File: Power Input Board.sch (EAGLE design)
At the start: 9 parts, among them Q1 SPB80P06P

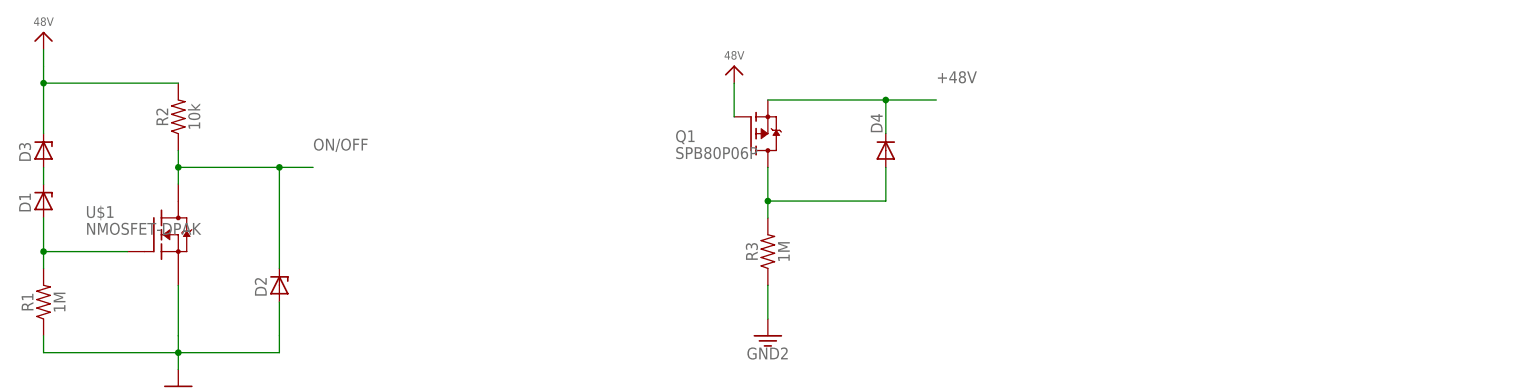
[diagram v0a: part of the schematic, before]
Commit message: added board outline
added the board outline
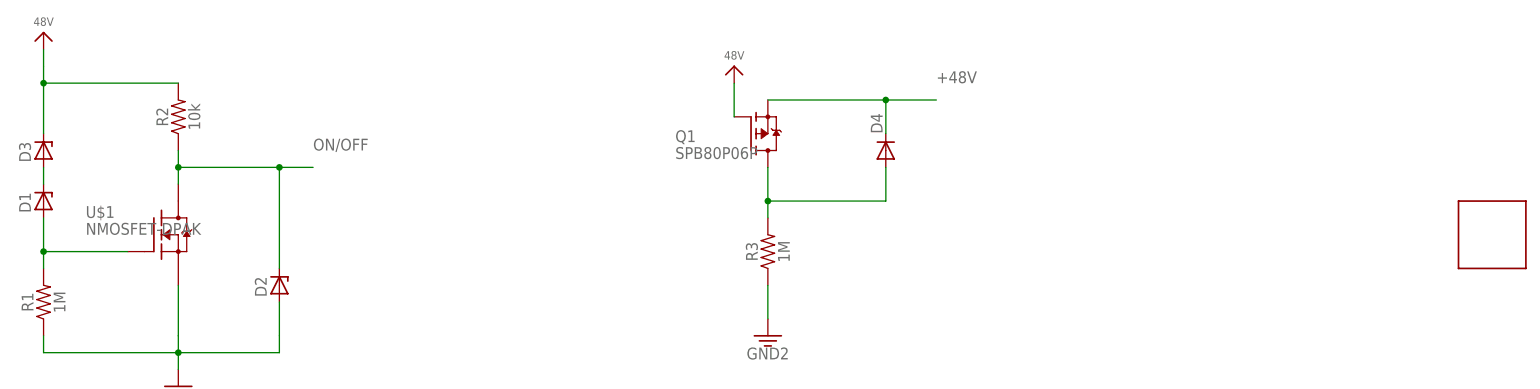
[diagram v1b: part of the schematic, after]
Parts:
- added U$2: BOARDPDB, board_outlines:BOARDPDB
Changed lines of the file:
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@@
 <?xml version="1.0" encoding="utf-8"?>
 <!DOCTYPE eagle SYSTEM "eagle.dtd">
-<eagle version="9.1.3">
+<eagle version="9.2.0">
 <drawing>
 <settings>
@@
 <part name="+48V" library="audio amplifier example" library_urn="urn:adsk.eagle:library:970892" deviceset="VCC" device="" value="48V"/>
 <part name="Q1" library="transistor-fet" library_urn="urn:adsk.eagle:library:396" deviceset="SPB80P06P" device="" package3d_urn="urn:adsk.eagle:package:28539/2"/>
+<part name="U$2" library="board_outlines" deviceset="BOARD" device="PDB"/>
 </parts>
 <sheets>
@@
 </plain>
 <instances>
-<instance part="U$1" gate="G$1" x="55.88" y="198.12"/>
-<instance part="D1" gate="G$1" x="38.1" y="203.2" rot="R90"/>
-<instance part="D2" gate="G$1" x="73.66" y="190.5" rot="R90"/>
-<instance part="D3" gate="G$1" x="38.1" y="210.82" rot="R90"/>
-<instance part="R1" gate="G$1" x="38.1" y="187.96" rot="R90"/>
-<instance part="R2" gate="G$1" x="58.42" y="215.9" rot="R90"/>
-<instance part="FRAME1" gate="G$1" x="0" y="0"/>
-<instance part="P+1" gate="VCC" x="38.1" y="228.6"/>
-<instance part="GND1" gate="G$1" x="58.42" y="175.26"/>
-<instance part="D4" gate="G$1" x="165.1" y="210.82" rot="R90"/>
-<instance part="R3" gate="G$1" x="147.32" y="195.58" rot="R90"/>
-<instance part="GND2" gate="G$1" x="147.32" y="182.88"/>
-<instance part="+48V" gate="VCC" x="142.24" y="223.52"/>
-<instance part="Q1" gate="G$1" x="144.78" y="213.36"/>
+<instance part="U$1" gate="G$1" x="55.88" y="198.12">
+<attribute name="VALUE" x="44.45" y="198.12" size="1.778" layer="96"/>
+<attribute name="NAME" x="44.45" y="200.66" size="1.778" layer="95"/>
+</instance>
+<instance part="D1" gate="G$1" x="38.1" y="203.2" rot="R90">
+<attribute name="NAME" x="36.195" y="201.422" size="1.778" layer="95" rot="R90"/>
+<attribute name="VALUE" x="41.529" y="201.422" size="1.778" layer="96" rot="R90"/>
+</instance>
+<instance part="D2" gate="G$1" x="73.66" y="190.5" rot="R90">
+<attribute name="NAME" x="71.755" y="188.722" size="1.778" layer="95" rot="R90"/>
+<attribute name="VALUE" x="77.089" y="188.722" size="1.778" layer="96" rot="R90"/>
+</instance>
+<instance part="D3" gate="G$1" x="38.1" y="210.82" rot="R90">
+<attribute name="NAME" x="36.195" y="209.042" size="1.778" layer="95" rot="R90"/>
+<attribute name="VALUE" x="41.529" y="209.042" size="1.778" layer="96" rot="R90"/>
+</instance>
+<instance part="R1" gate="G$1" x="38.1" y="187.96" rot="R90">
+<attribute name="NAME" x="36.576" y="187.96" size="1.778" layer="95" font="vector" rot="R90" align="bottom-center"/>
+<attribute name="VALUE" x="39.624" y="187.96" size="1.778" layer="96" font="vector" rot="R90" align="top-center"/>
+</instance>
+<instance part="R2" gate="G$1" x="58.42" y="215.9" rot="R90">
+<attribute name="NAME" x="56.896" y="215.9" size="1.778" layer="95" font="vector" rot="R90" align="bottom-center"/>
+<attribute name="VALUE" x="59.944" y="215.9" size="1.778" layer="96" font="vector" rot="R90" align="top-center"/>
+</instance>
+<instance part="FRAME1" gate="G$1" x="0" y="0">
+<attribute name="DRAWING_NAME" x="344.17" y="15.24" size="2.54" layer="94"/>
+<attribute name="LAST_DATE_TIME" x="344.17" y="10.16" size="2.286" layer="94"/>
+<attribute name="SHEET" x="357.505" y="5.08" size="2.54" layer="94"/>
+</instance>
+<instance part="P+1" gate="VCC" x="38.1" y="228.6">
+<attribute name="VALUE" x="36.576" y="229.616" size="1.27" layer="96"/>
+</instance>
+<instance part="GND1" gate="G$1" x="58.42" y="175.26">
+<attribute name="VALUE" x="58.42" y="173.482" size="1.778" layer="96" align="top-center"/>
+</instance>
+<instance part="D4" gate="G$1" x="165.1" y="210.82" rot="R90">
+<attribute name="NAME" x="164.6174" y="213.36" size="1.778" layer="95" rot="R90"/>
+<attribute name="VALUE" x="167.4114" y="213.36" size="1.778" layer="96" rot="R90"/>
+</instance>
+<instance part="R3" gate="G$1" x="147.32" y="195.58" rot="R90">
+<attribute name="NAME" x="145.796" y="195.58" size="1.778" layer="95" font="vector" rot="R90" align="bottom-center"/>
+<attribute name="VALUE" x="148.844" y="195.58" size="1.778" layer="96" font="vector" rot="R90" align="top-center"/>
+</instance>
+<instance part="GND2" gate="G$1" x="147.32" y="182.88">
+<attribute name="VALUE" x="147.32" y="181.102" size="1.778" layer="96" align="top-center"/>
+</instance>
+<instance part="+48V" gate="VCC" x="142.24" y="223.52">
+<attribute name="VALUE" x="140.716" y="224.536" size="1.27" layer="96"/>
+</instance>
+<instance part="Q1" gate="G$1" x="144.78" y="213.36">
+<attribute name="VALUE" x="133.35" y="209.55" size="1.778" layer="96"/>
+<attribute name="NAME" x="133.35" y="212.09" size="1.778" layer="95"/>
+</instance>
+<instance part="U$2" gate="G$1" x="256.54" y="198.12"/>
 </instances>
 <busses>

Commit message: put in outline
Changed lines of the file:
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@@
 <attribute name="NAME" x="133.35" y="212.09" size="1.778" layer="95"/>
 </instance>
-<instance part="U$2" gate="G$1" x="256.54" y="198.12"/>
+<instance part="U$2" gate="G$1" x="215.9" y="241.3"/>
 </instances>
 <busses>

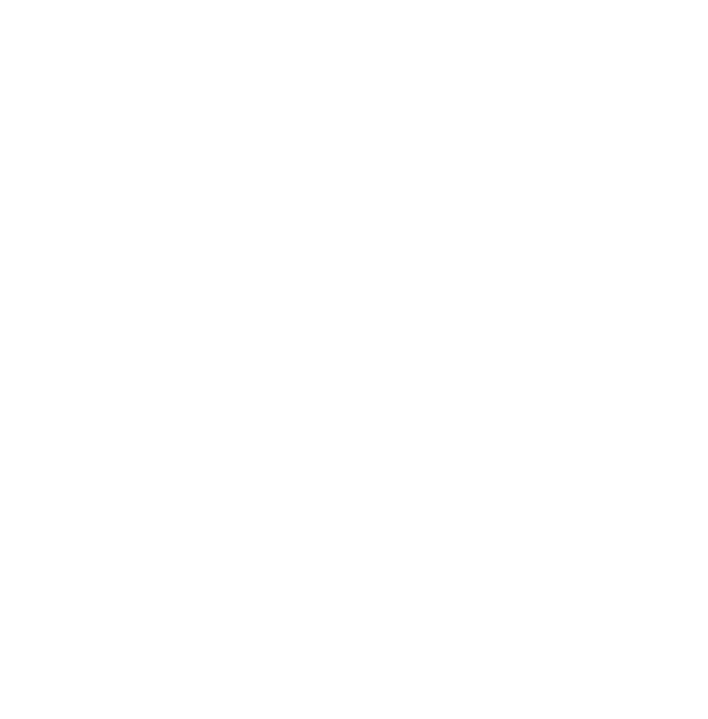
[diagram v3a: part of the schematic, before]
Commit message: inserted diodes
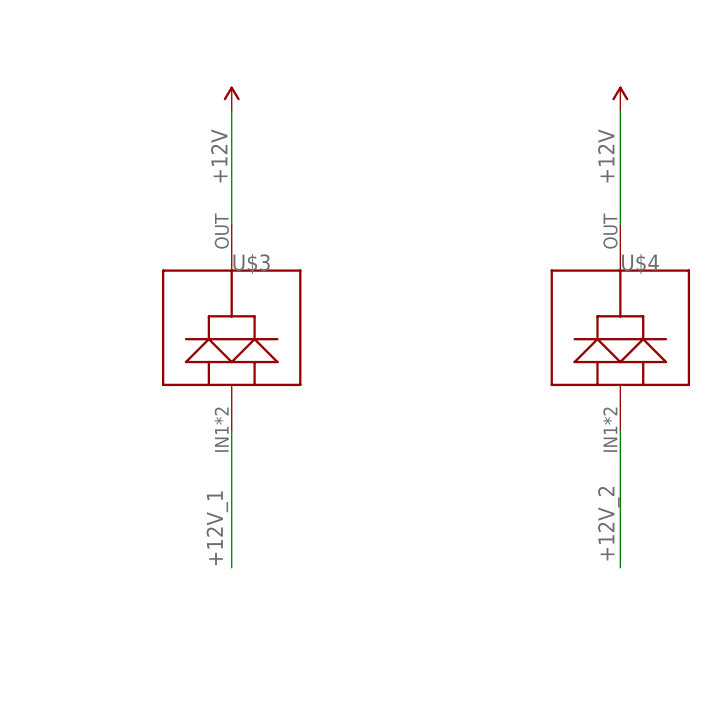
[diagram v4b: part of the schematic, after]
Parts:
- added U$3, U$4: DIODE, DIODE:DIODE
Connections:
- new net +12V: U$3.OUT, U$4.OUT
- new net +12V_1: U$3.IN2
- new net +12V_2: U$4.IN2
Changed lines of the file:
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@@
 <setting verticaltext="up"/>
 </settings>
-<grid distance="0.1" unitdist="inch" unit="inch" style="lines" multiple="1" display="no" altdistance="0.01" altunitdist="inch" altunit="inch"/>
+<grid distance="1" unitdist="mm" unit="mm" style="lines" multiple="1" display="no" altdistance="0.01" altunitdist="inch" altunit="inch"/>
 <layers>
 <layer number="1" name="Top" color="4" fill="1" visible="no" active="no"/>
@@
 <part name="Q1" library="transistor-fet" library_urn="urn:adsk.eagle:library:396" deviceset="SPB80P06P" device="" package3d_urn="urn:adsk.eagle:package:28539/2"/>
 <part name="U$2" library="board_outlines" deviceset="BOARD" device="PDB"/>
+<part name="U$3" library="DIODE" deviceset="DIODE" device=""/>
+<part name="U$4" library="DIODE" deviceset="DIODE" device=""/>
+<part name="SUPPLY1" library="SparkFun-PowerSymbols" library_urn="urn:adsk.eagle:library:530" deviceset="VCC" device="" value=""/>
+<part name="SUPPLY2" library="SparkFun-PowerSymbols" library_urn="urn:adsk.eagle:library:530" deviceset="VCC" device="" value=""/>
 </parts>
 <sheets>
@@
 </instance>
 <instance part="U$2" gate="G$1" x="215.9" y="241.3"/>
+<instance part="U$3" gate="G$1" x="284.48" y="213.36"/>
+<instance part="U$4" gate="G$1" x="327.66" y="213.36"/>
+<instance part="SUPPLY1" gate="G$1" x="284.48" y="236.22"/>
+<instance part="SUPPLY2" gate="G$1" x="327.66" y="236.22"/>
 </instances>
 <busses>
@@
 </segment>
 </net>
+<net name="+12V_1" class="0">
+<segment>
+<pinref part="U$3" gate="G$1" pin="IN2"/>
+<wire x1="284.48" y1="200.66" x2="284.48" y2="185.42" width="0.1524" layer="91"/>
+<label x="283.5" y="185.48" size="1.778" layer="95" rot="R90"/>
+</segment>
+</net>
+<net name="+12V_2" class="0">
+<segment>
+<pinref part="U$4" gate="G$1" pin="IN2"/>
+<wire x1="327.66" y1="200.66" x2="327.66" y2="185.42" width="0.1524" layer="91"/>
+<label x="327" y="186" size="1.778" layer="95" rot="R90"/>
+</segment>
+</net>
+<net name="+12V" class="0">
+<segment>
+<pinref part="U$3" gate="G$1" pin="OUT"/>
+<wire x1="284.48" y1="223.52" x2="284.48" y2="236.22" width="0.1524" layer="91"/>
+<pinref part="SUPPLY1" gate="G$1" pin="VCC"/>
+<label x="284" y="228" size="1.778" layer="95" rot="R90"/>
+</segment>
+<segment>
+<pinref part="U$4" gate="G$1" pin="OUT"/>
+<wire x1="327.66" y1="223.52" x2="327.66" y2="236.22" width="0.1524" layer="91"/>
+<pinref part="SUPPLY2" gate="G$1" pin="VCC"/>
+<label x="327" y="228" size="1.778" layer="95" rot="R90"/>
+</segment>
+</net>

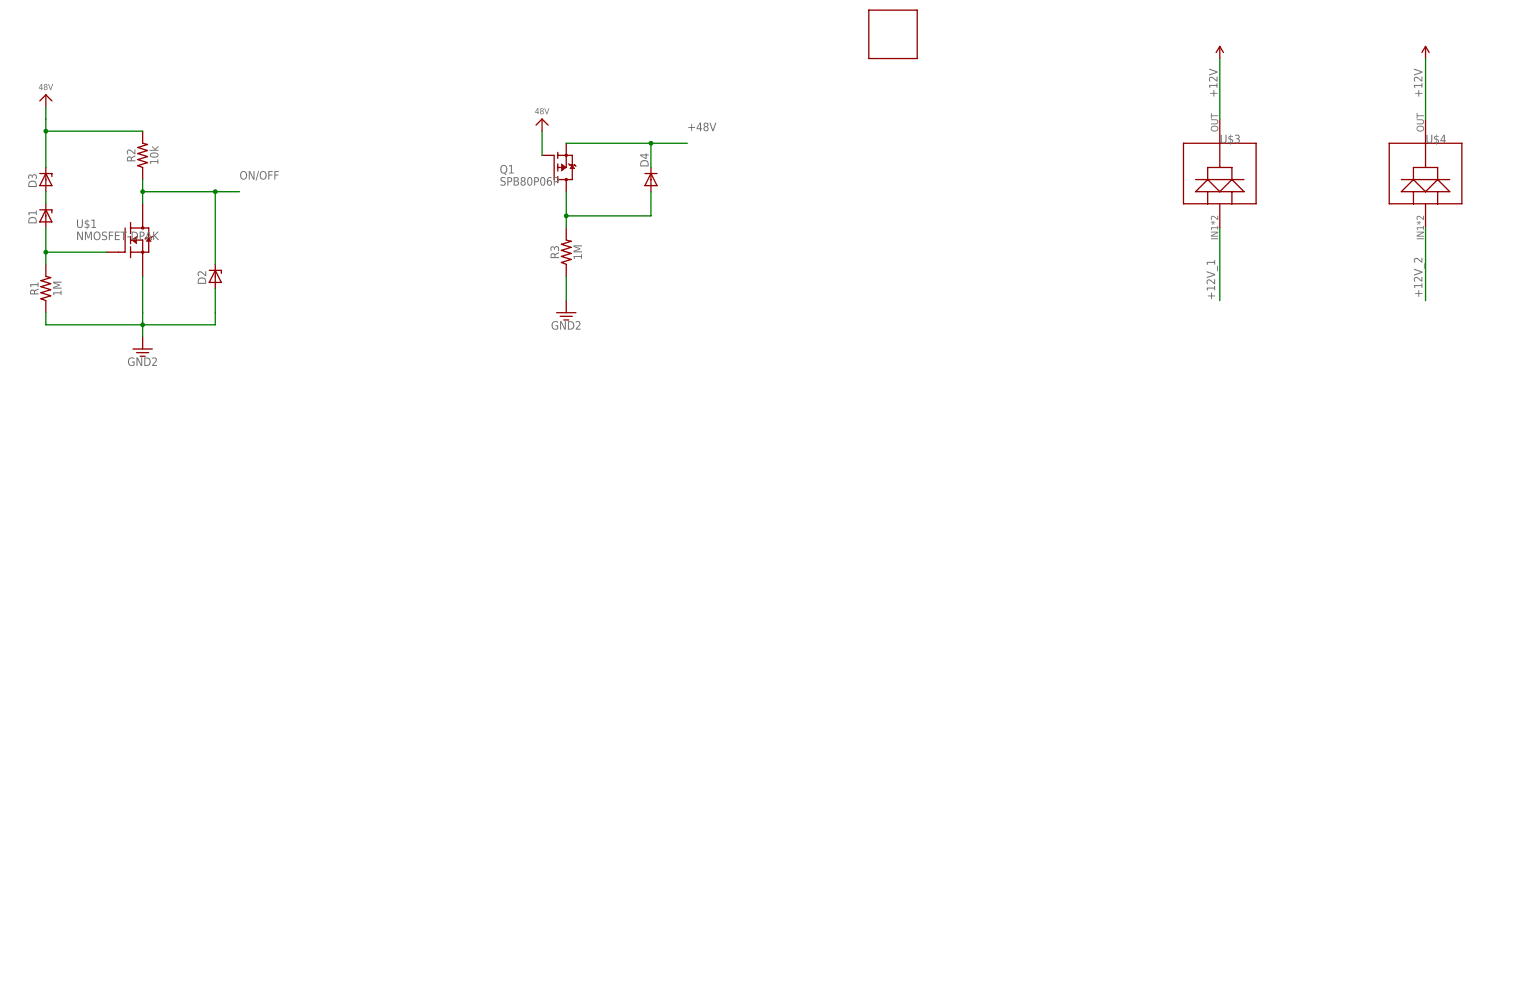
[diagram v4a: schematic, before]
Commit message: put the connectors on the board
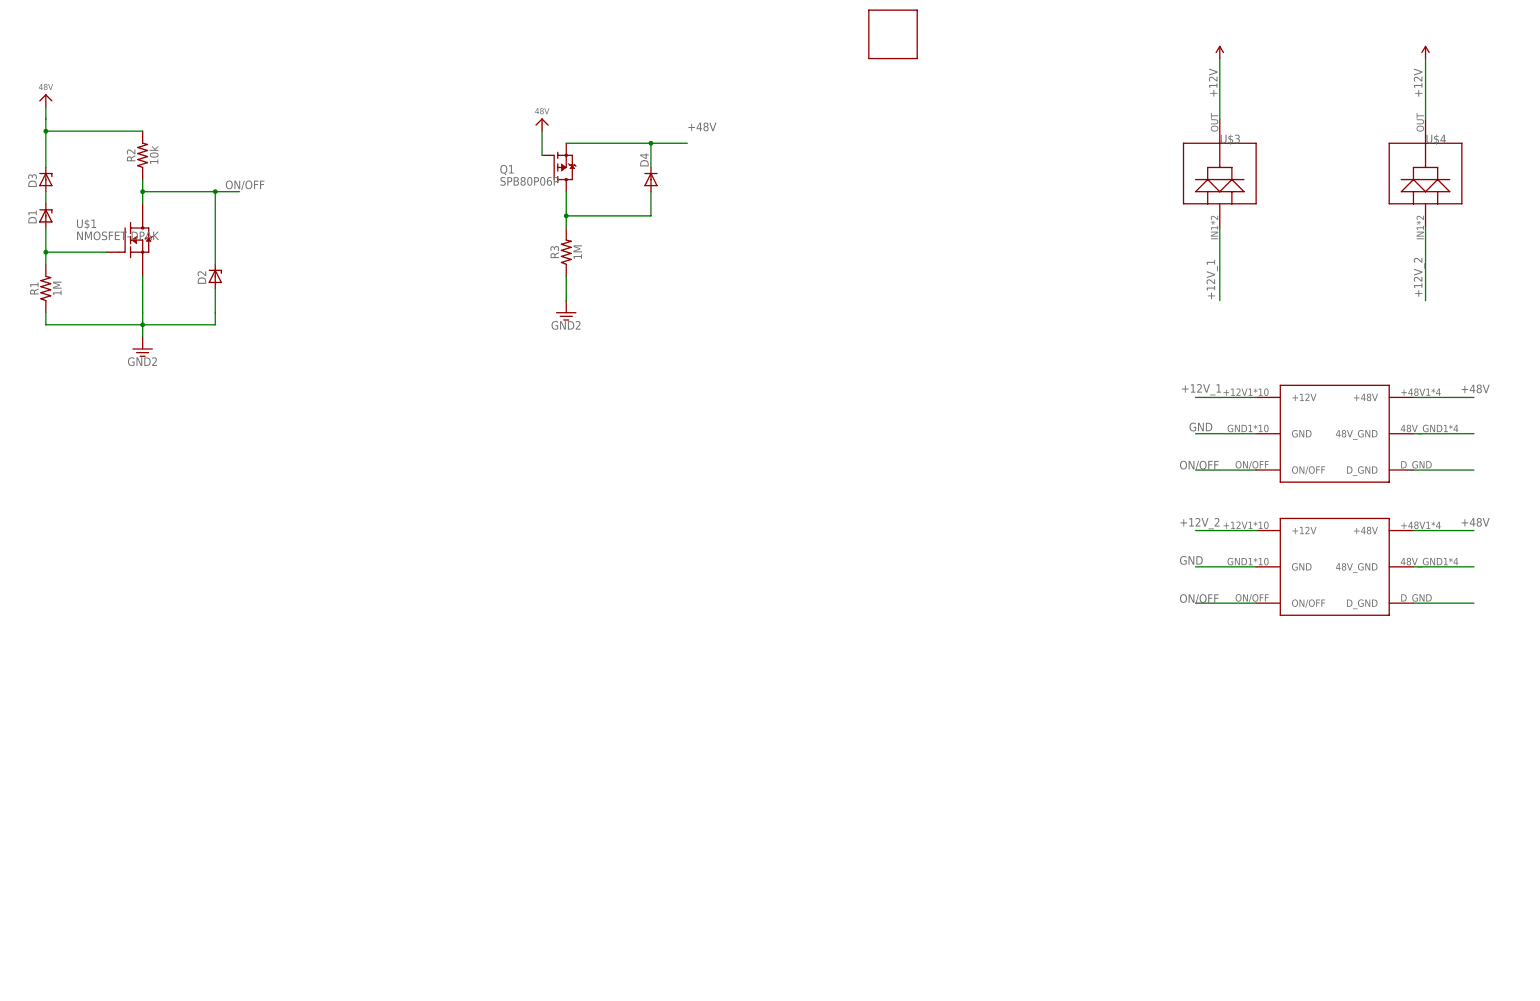
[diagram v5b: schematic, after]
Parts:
- added U$5, U$6: BRICK_TO_POWER_DIST_WHOLE, PDB_TO_BRICKS:BRICK_TO_POWER_DIST_WHOLE
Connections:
- new net GND: U$5.GND, U$6.GND
- new net N$10: U$5.D_GND
- new net N$12: U$6.48V_GND
- new net N$13: U$6.D_GND
- new net N$9: U$5.48V_GND
- net +12V_1: now also U$5.+12V
- net +12V_2: now also U$6.+12V
- net +48V: now also U$5.+48V, U$6.+48V
- net ON/OFF: now also U$5.ON/OFF, U$6.ON/OFF
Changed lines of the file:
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@@
 <part name="SUPPLY1" library="SparkFun-PowerSymbols" library_urn="urn:adsk.eagle:library:530" deviceset="VCC" device="" value=""/>
 <part name="SUPPLY2" library="SparkFun-PowerSymbols" library_urn="urn:adsk.eagle:library:530" deviceset="VCC" device="" value=""/>
+<part name="U$5" library="PDB_TO_BRICKS" deviceset="BRICK_TO_POWER_DIST_WHOLE" device=""/>
+<part name="U$6" library="PDB_TO_BRICKS" deviceset="BRICK_TO_POWER_DIST_WHOLE" device=""/>
 </parts>
 <sheets>
@@
 <instance part="SUPPLY1" gate="G$1" x="284.48" y="236.22"/>
 <instance part="SUPPLY2" gate="G$1" x="327.66" y="236.22"/>
+<instance part="U$5" gate="G$1" x="297.18" y="147.32"/>
+<instance part="U$6" gate="G$1" x="297.18" y="119.38"/>
 </instances>
 <busses>
@@
 <wire x1="73.66" y1="208.28" x2="78.74" y2="208.28" width="0.1524" layer="91"/>
 <junction x="73.66" y="208.28"/>
-<label x="78.74" y="210.82" size="1.778" layer="95"/>
+<label x="75.74" y="208.82" size="1.778" layer="95"/>
+</segment>
+<segment>
+<pinref part="U$5" gate="G$1" pin="ON/OFF"/>
+<wire x1="292.1" y1="149.86" x2="279.4" y2="149.86" width="0.1524" layer="91"/>
+<label x="276" y="150" size="1.778" layer="95"/>
+</segment>
+<segment>
+<pinref part="U$6" gate="G$1" pin="ON/OFF"/>
+<wire x1="292.1" y1="121.92" x2="279.4" y2="121.92" width="0.1524" layer="91"/>
+<label x="276" y="122" size="1.778" layer="95"/>
 </segment>
 </net>
@@
 <junction x="165.1" y="218.44"/>
 </segment>
+<segment>
+<pinref part="U$5" gate="G$1" pin="+48V"/>
+<wire x1="325.12" y1="165.1" x2="337.82" y2="165.1" width="0.1524" layer="91"/>
+<label x="335" y="166" size="1.778" layer="95"/>
+</segment>
+<segment>
+<pinref part="U$6" gate="G$1" pin="+48V"/>
+<wire x1="325.12" y1="137.16" x2="337.82" y2="137.16" width="0.1524" layer="91"/>
+<label x="335" y="138" size="1.778" layer="95"/>
+</segment>
 </net>
 <net name="VCC" class="0">
@@
 <label x="283.5" y="185.48" size="1.778" layer="95" rot="R90"/>
 </segment>
+<segment>
+<pinref part="U$5" gate="G$1" pin="+12V"/>
+<wire x1="292.1" y1="165.1" x2="279.4" y2="165.1" width="0.1524" layer="91"/>
+<label x="276.32" y="166.1" size="1.778" layer="95"/>
+</segment>
 </net>
 <net name="+12V_2" class="0">
@@
 <wire x1="327.66" y1="200.66" x2="327.66" y2="185.42" width="0.1524" layer="91"/>
 <label x="327" y="186" size="1.778" layer="95" rot="R90"/>
+</segment>
+<segment>
+<pinref part="U$6" gate="G$1" pin="+12V"/>
+<wire x1="292.1" y1="137.16" x2="279.4" y2="137.16" width="0.1524" layer="91"/>
+<label x="276" y="138" size="1.778" layer="95"/>
 </segment>
 </net>
@@
 </segment>
 </net>
+<net name="GND" class="0">
+<segment>
+<pinref part="U$5" gate="G$1" pin="GND"/>
+<wire x1="292.1" y1="157.48" x2="279.4" y2="157.48" width="0.1524" layer="91"/>
+<label x="278" y="158" size="1.778" layer="95"/>
+</segment>
+<segment>
+<pinref part="U$6" gate="G$1" pin="GND"/>
+<wire x1="292.1" y1="129.54" x2="279.4" y2="129.54" width="0.1524" layer="91"/>
+<label x="276" y="130" size="1.778" layer="95"/>
+</segment>
+</net>
+<net name="N$9" class="0">
+<segment>
+<pinref part="U$5" gate="G$1" pin="48V_GND"/>
+<wire x1="325.12" y1="157.48" x2="337.82" y2="157.48" width="0.1524" layer="91"/>
+</segment>
+</net>
+<net name="N$10" class="0">
+<segment>
+<pinref part="U$5" gate="G$1" pin="D_GND"/>
+<wire x1="325.12" y1="149.86" x2="337.82" y2="149.86" width="0.1524" layer="91"/>
+</segment>
+</net>
+<net name="N$12" class="0">
+<segment>
+<pinref part="U$6" gate="G$1" pin="48V_GND"/>
+<wire x1="325.12" y1="129.54" x2="337.82" y2="129.54" width="0.1524" layer="91"/>
+</segment>
+</net>
+<net name="N$13" class="0">
+<segment>
+<pinref part="U$6" gate="G$1" pin="D_GND"/>
+<wire x1="325.12" y1="121.92" x2="337.82" y2="121.92" width="0.1524" layer="91"/>
+</segment>
+</net>
